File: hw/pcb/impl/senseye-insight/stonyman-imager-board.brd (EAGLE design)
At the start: 14.9 x 16.4 mm, 10 parts, among them J1 HEADER_12PIN2X6_NOSILK, U1 STONYMANDEFAULT_LENS_MOUNT, U2 TI_ADCXX1S101

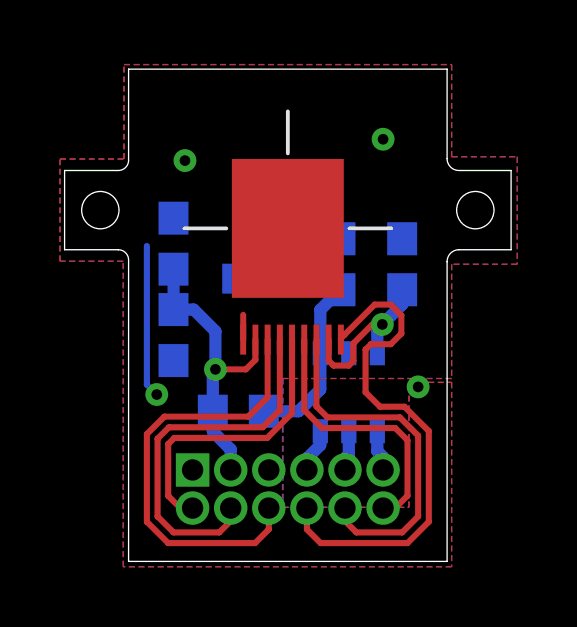
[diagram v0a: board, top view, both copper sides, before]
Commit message: added larger via with soldermask for ANALOG
this is a more accessable test point for the ANALOG signal.  It doesn't
alter the board design much, it's just a tad bigger.  Signals were
re-routed around it.

Also expanded the ground planes to fill in the area under the ADC.
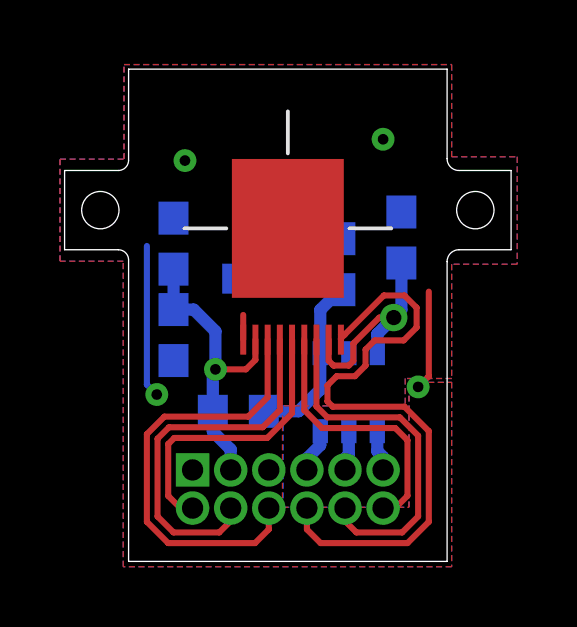
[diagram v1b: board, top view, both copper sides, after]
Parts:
- moved C5 0.89 mm to (11.2, 10.8)
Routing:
- net OENABLE: track 17.2 -> 20.8 mm
- net GND: track 5.91 -> 9.24 mm
- net ANALOG: track 5.93 -> 7.28 mm
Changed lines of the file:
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@@
 <setting verticaltext="up"/>
 </settings>
-<grid distance="0.1" unitdist="inch" unit="inch" style="lines" multiple="1" display="yes" altdistance="0.01" altunitdist="inch" altunit="inch"/>
+<grid distance="0.1" unitdist="inch" unit="inch" style="lines" multiple="1" display="yes" altdistance="0.001" altunitdist="inch" altunit="inch"/>
 <layers>
 <layer number="1" name="Top" color="4" fill="1" visible="yes" active="yes"/>
@@
 <attribute name="VALUE" x="12.6492" y="1.016" size="1.016" layer="27" font="vector" ratio="12" rot="R90"/>
 </element>
-<element name="C5" library="rcl" package="C0603" value="OPTIONAL: 10pF-1nF" x="11.2522" y="9.906" smashed="yes" rot="MR90">
-<attribute name="NAME" x="10.2616" y="12.192" size="0.762" layer="26" rot="SMR180"/>
-<attribute name="VALUE" x="9.3472" y="9.271" size="1.27" layer="28" rot="MR90"/>
+<element name="C5" library="rcl" package="C0603" value="OPTIONAL: 10pF-1nF" x="11.2268" y="10.795" smashed="yes" rot="MR90">
+<attribute name="NAME" x="10.2362" y="13.081" size="0.762" layer="26" rot="SMR180"/>
+<attribute name="VALUE" x="9.3218" y="10.16" size="1.27" layer="28" rot="MR90"/>
 </element>
 <element name="U$1" library="logos" package="UMICH_SOLID_75MIL" value="UMICH_SOLID_SMALL" x="5.334" y="13.2588" rot="SMR180"/>
@@
 <vertex x="12.9032" y="9.906"/>
 <vertex x="12.9032" y="6.096"/>
-<vertex x="7.2644" y="6.096"/>
+<vertex x="11.3538" y="6.096"/>
+<vertex x="11.3538" y="5.1816"/>
+<vertex x="7.2644" y="5.1816"/>
 <vertex x="7.2644" y="1.8034"/>
 <vertex x="11.4808" y="1.8034"/>
@@
 <vertex x="12.9032" y="9.906"/>
 <vertex x="12.9032" y="6.096"/>
-<vertex x="7.2898" y="6.096"/>
+<vertex x="11.3538" y="6.096"/>
+<vertex x="11.3538" y="5.1816"/>
+<vertex x="7.2898" y="5.1816"/>
 <vertex x="7.2898" y="1.8034"/>
 <vertex x="11.4808" y="1.8034"/>
@@
 <contactref element="C3" pad="2"/>
 <contactref element="C4" pad="2"/>
+<wire x1="11.7856" y1="5.8166" x2="12.1412" y2="6.1722" width="0.2032" layer="1"/>
+<wire x1="12.1412" y1="6.1722" x2="12.1412" y2="8.9916" width="0.2032" layer="1"/>
 </signal>
 <signal name="V_STONY">
@@
 <wire x1="8.5344" y1="0.6096" x2="8.0772" y2="1.0668" width="0.2032" layer="1"/>
 <wire x1="8.0772" y1="1.0668" x2="8.0772" y2="1.778" width="0.2032" layer="1"/>
-<wire x1="9.2108" y1="7.5598" x2="9.3378" y2="7.5598" width="0.2032" layer="1"/>
-<wire x1="9.3378" y1="7.5598" x2="10.3378" y2="8.5598" width="0.2032" layer="1"/>
-<wire x1="10.3378" y1="8.5598" x2="10.8712" y2="8.5598" width="0.2032" layer="1"/>
-<wire x1="10.8712" y1="8.5598" x2="11.2268" y2="8.2042" width="0.2032" layer="1"/>
-<wire x1="11.2268" y1="8.2042" x2="11.2268" y2="7.5946" width="0.2032" layer="1"/>
-<wire x1="11.2268" y1="7.5946" x2="10.8712" y2="7.239" width="0.2032" layer="1"/>
-<wire x1="10.8712" y1="7.239" x2="10.2108" y2="7.239" width="0.2032" layer="1"/>
-<wire x1="10.2108" y1="7.239" x2="10.033" y2="7.0612" width="0.2032" layer="1"/>
-<wire x1="10.033" y1="7.0612" x2="10.033" y2="5.6388" width="0.2032" layer="1"/>
-<wire x1="10.033" y1="5.6388" x2="10.5156" y2="5.1562" width="0.2032" layer="1"/>
-<wire x1="10.5156" y1="5.1562" x2="11.3284" y2="5.1562" width="0.2032" layer="1"/>
+<wire x1="9.3378" y1="7.5598" x2="10.6426" y2="8.8646" width="0.2032" layer="1"/>
 <wire x1="11.3284" y1="5.1562" x2="12.1412" y2="4.3434" width="0.2032" layer="1"/>
 <wire x1="9.3378" y1="7.5598" x2="9.2108" y2="7.4328" width="0.2032" layer="1"/>
 <wire x1="9.2108" y1="7.4328" x2="9.2108" y2="7.3924" width="0.2032" layer="1"/>
+<wire x1="9.2108" y1="7.5598" x2="9.3378" y2="7.5598" width="0.2032" layer="1"/>
+<wire x1="10.6426" y1="8.8646" x2="11.3284" y2="8.8646" width="0.2032" layer="1"/>
+<wire x1="11.3284" y1="8.8646" x2="11.7348" y2="8.4582" width="0.2032" layer="1"/>
+<wire x1="11.7348" y1="8.4582" x2="11.7348" y2="7.7978" width="0.2032" layer="1"/>
+<wire x1="11.7348" y1="7.7978" x2="11.303" y2="7.366" width="0.2032" layer="1"/>
+<wire x1="11.303" y1="7.366" x2="10.3378" y2="7.366" width="0.2032" layer="1"/>
+<wire x1="10.3378" y1="7.366" x2="10.033" y2="7.0612" width="0.2032" layer="1"/>
+<wire x1="10.033" y1="7.0612" x2="10.033" y2="6.5278" width="0.2032" layer="1"/>
+<wire x1="10.033" y1="6.5278" x2="9.6774" y2="6.1722" width="0.2032" layer="1"/>
+<wire x1="8.763" y1="5.334" x2="8.9408" y2="5.1562" width="0.2032" layer="1"/>
+<wire x1="9.6774" y1="6.1722" x2="9.0678" y2="6.1722" width="0.2032" layer="1"/>
+<wire x1="9.0678" y1="6.1722" x2="8.763" y2="5.8674" width="0.2032" layer="1"/>
+<wire x1="8.763" y1="5.8674" x2="8.763" y2="5.334" width="0.2032" layer="1"/>
+<wire x1="8.9408" y1="5.1562" x2="11.3284" y2="5.1562" width="0.2032" layer="1"/>
 </signal>
 <signal name="V_ADC">
@@
 <signal name="ANALOG">
 <contactref element="U1" pad="P$8"/>
-<via x="10.5918" y="7.8994" extent="1-16" drill="0.3556" diameter="0.254"/>
 <wire x1="8.8038" y1="7.3924" x2="8.8038" y2="6.6902" width="0.2032" layer="1"/>
 <wire x1="8.8038" y1="6.6902" x2="8.9662" y2="6.5278" width="0.2032" layer="1"/>
@@
 <wire x1="9.4742" y1="6.5278" x2="9.6266" y2="6.6802" width="0.2032" layer="1"/>
 <wire x1="9.6266" y1="6.6802" x2="9.6266" y2="7.2644" width="0.2032" layer="1"/>
-<wire x1="9.6266" y1="7.2644" x2="10.2616" y2="7.8994" width="0.2032" layer="1"/>
-<wire x1="10.2616" y1="7.8994" x2="10.5918" y2="7.8994" width="0.2032" layer="1"/>
 <contactref element="C5" pad="1"/>
 <contactref element="U2" pad="3"/>
-<wire x1="10.4242" y1="6.9388" x2="10.4242" y2="7.7318" width="0.4064" layer="16"/>
-<wire x1="10.4242" y1="7.7318" x2="10.5918" y2="7.8994" width="0.4064" layer="16"/>
-<wire x1="10.5918" y1="7.8994" x2="11.2522" y2="8.5598" width="0.4064" layer="16"/>
-<wire x1="11.2522" y1="8.5598" x2="11.2522" y2="9.056" width="0.4064" layer="16"/>
+<via x="10.9728" y="8.128" extent="1-16" drill="0.508"/>
+<wire x1="9.6266" y1="7.2644" x2="10.4902" y2="8.128" width="0.2032" layer="1"/>
+<wire x1="10.4902" y1="8.128" x2="10.9728" y2="8.128" width="0.2032" layer="1"/>
+<wire x1="10.9728" y1="8.128" x2="11.2268" y2="8.382" width="0.4064" layer="16"/>
+<wire x1="11.2268" y1="8.382" x2="11.2268" y2="9.945" width="0.4064" layer="16"/>
+<wire x1="10.4242" y1="6.9388" x2="10.4242" y2="7.5794" width="0.4064" layer="16"/>
+<wire x1="10.4242" y1="7.5794" x2="10.9728" y2="8.128" width="0.4064" layer="16"/>
 </signal>
 <signal name="ADC-MISO">

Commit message: expanded distance between headers and lens mount
in the board file for the stonyman-imager-board.  Also, updated the date
on the silkscreen to today's date.
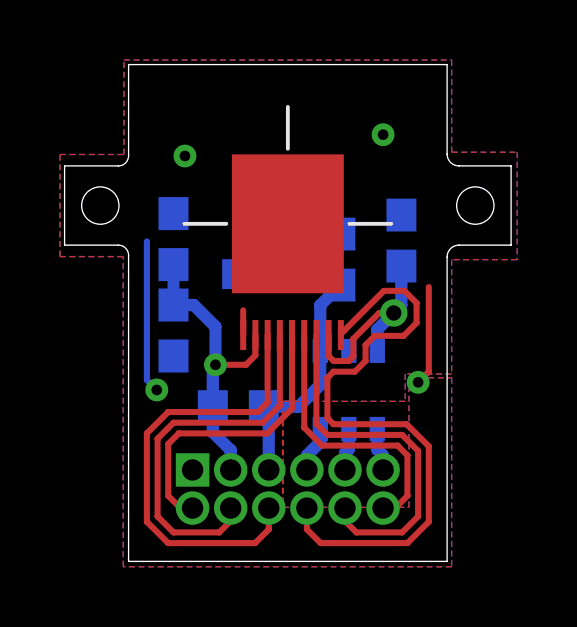
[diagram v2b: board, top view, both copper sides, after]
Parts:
- moved C1 0.15 mm to (3.63, 10.7)
- moved C2 0.15 mm to (3.63, 7.70)
- moved C3 0.15 mm to (9.19, 10.1)
- moved R1 0.15 mm to (5.79, 5.16)
- moved U1 0.15 mm to (7.44, 11.3)
- moved C4 0.15 mm to (6.65, 9.58)
- moved U$1 0.15 mm to (5.33, 13.4)
- moved C5 0.10 mm to (11.2, 10.7)
- moved U2 0.08 mm to (9.47, 5.71)
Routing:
- net V_ADC: track 7.86 -> 9.81 mm
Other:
- board size 14.9 x 16.4 mm -> 14.9 x 16.6 mm
- board text added: "10/28/2013"
- board text removed: "8/14/2013"
